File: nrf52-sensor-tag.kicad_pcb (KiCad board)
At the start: 2 copper layers, 36 x 36 mm, 20 parts, among them IC2 VEML6030, IC3 MS860702BA01-50, J3 Conn_01x07_Male, U1 MS88SF2

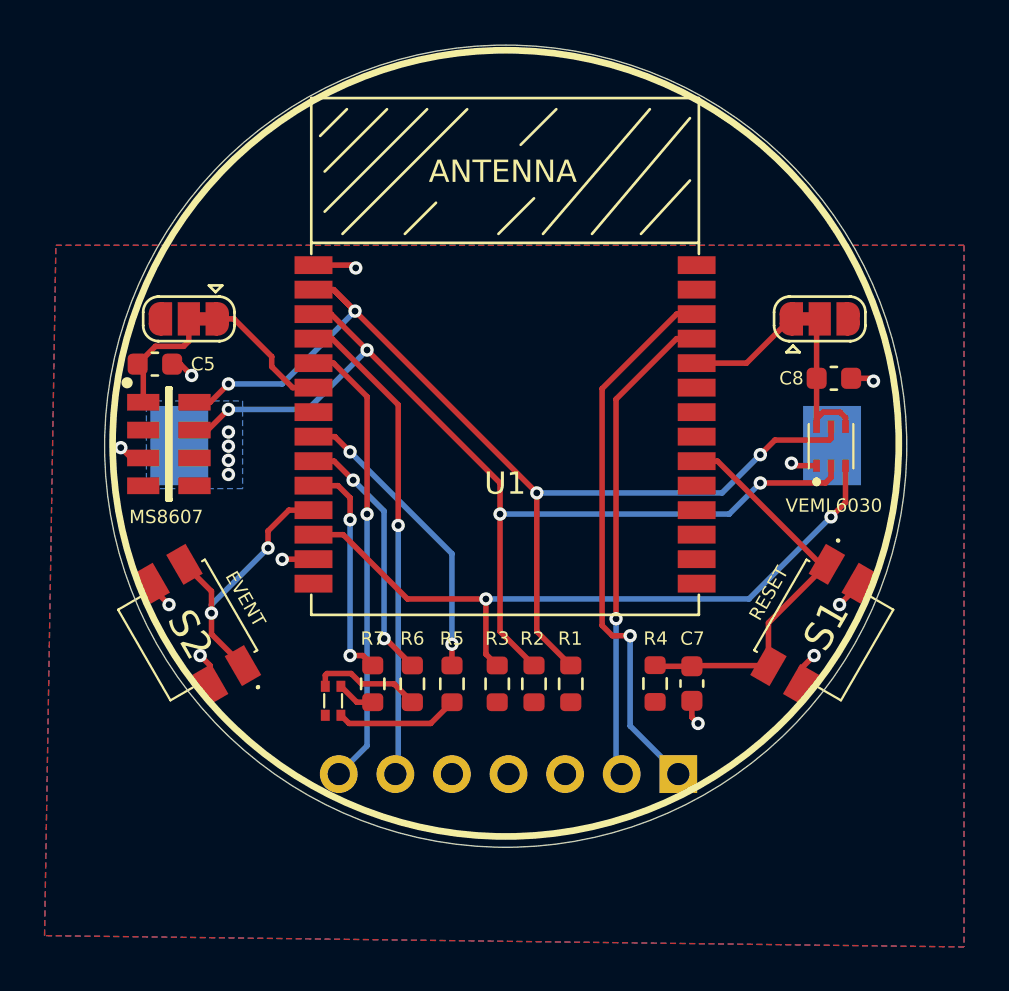
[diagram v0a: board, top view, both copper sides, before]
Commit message: #4 Sensor Tag improvements suggestions
https://github.com/HomeSmartMesh/nrf52_thread_sensortag/issues/4
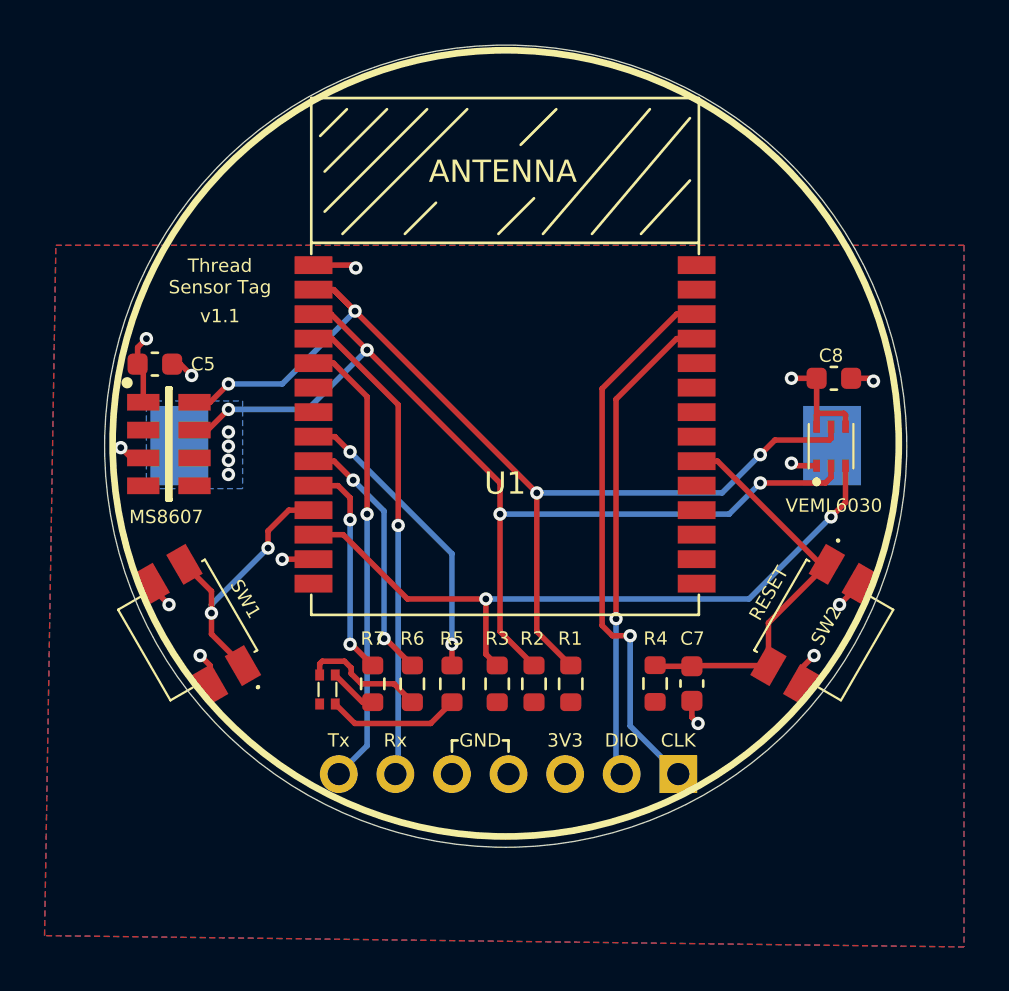
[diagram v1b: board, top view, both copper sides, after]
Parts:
- removed JP1, JP2: SolderJumper_3_Bridged12, Jumper:SolderJumper-3_P1.3mm_Bridged12_RoundedPad1.0x1.5mm
- moved LED1 0.57 mm to (113.8, 75.6)
- renumbered S2 to SW1, S1 to SW2
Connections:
- C5 pad 1: Net-(C5-Pad1) -> /VCC
- C8 pad 1: Net-(C8-Pad1) -> /VCC
- IC2 pad 4: Net-(C8-Pad1) -> /VCC
- IC2 pad 6: Net-(C8-Pad1) -> /VCC
- IC3 pad 1: Net-(C5-Pad1) -> /VCC
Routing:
- net /VCC: track 0.00 -> 8.84 mm, vias 4 -> 6
- net Net-(C8-Pad1): track 7.21 -> 0.00 mm
- net /SENS1_VCC: track 5.64 -> 0.00 mm
- net Net-(C5-Pad1): track 5.54 -> 0.00 mm
- net /SENS2_VCC: track 4.85 -> 0.00 mm
- net Net-(LED1-Pad4): track 4.97 -> 5.62 mm
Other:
- board text added: "CLK"
- board text added: "DIO"
- board text added: "SW1"
- board text removed: "DEBUG"
- board text removed: "EVENT"
- board text removed: "SWDCLK"
- board text removed: "SWDIO"
- board text removed: "UART"

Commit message: New edge cut + sensor turned by 68°
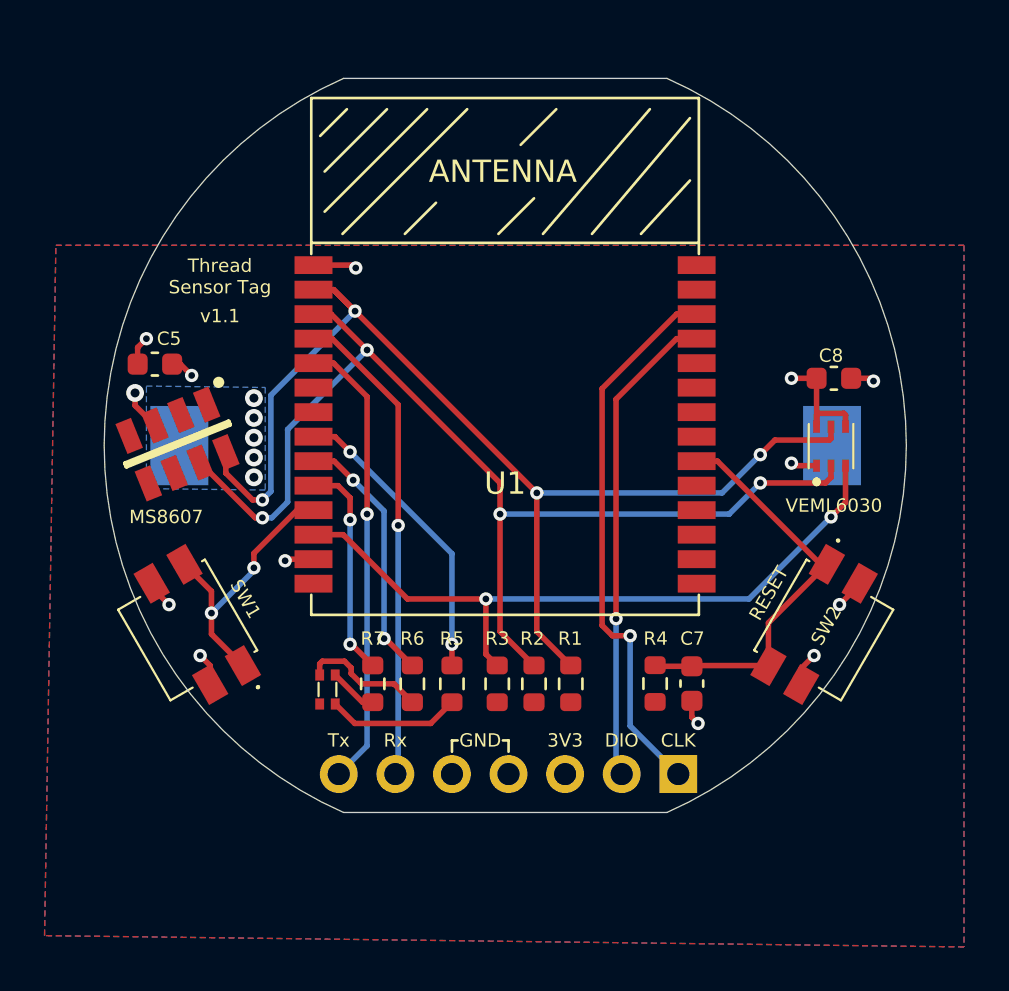
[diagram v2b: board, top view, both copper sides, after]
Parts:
- moved IC3 0.39 mm to (107.0, 64.5), turned to 292 degrees
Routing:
- net /SCL: track 47.4 -> 51.8 mm
- net /SDA: track 45.8 -> 50.2 mm
- net /VCC: track 8.84 -> 7.38 mm, vias 6 -> 7
- net GND: track 14.8 -> 15.4 mm
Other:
- board size 36 x 36 mm -> 36 x 33 mm

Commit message: Added Open Source Hardware Logo + Made in Germany + Designed with KiCad
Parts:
- added G***: LOGO, logo:mig, B.Cu at (117.9, 52.2)
- added REF**: KiCad-Logo2_5mm_SilkScreen, Symbol:KiCad-Logo2_5mm_SilkScreen, B.Cu at (122.1, 75.2)
- added REF**: OSHW-Symbol_6.7x6mm_SilkScreen, Symbol:OSHW-Symbol_6.7x6mm_SilkScreen, B.Cu at (125.9, 52.0)

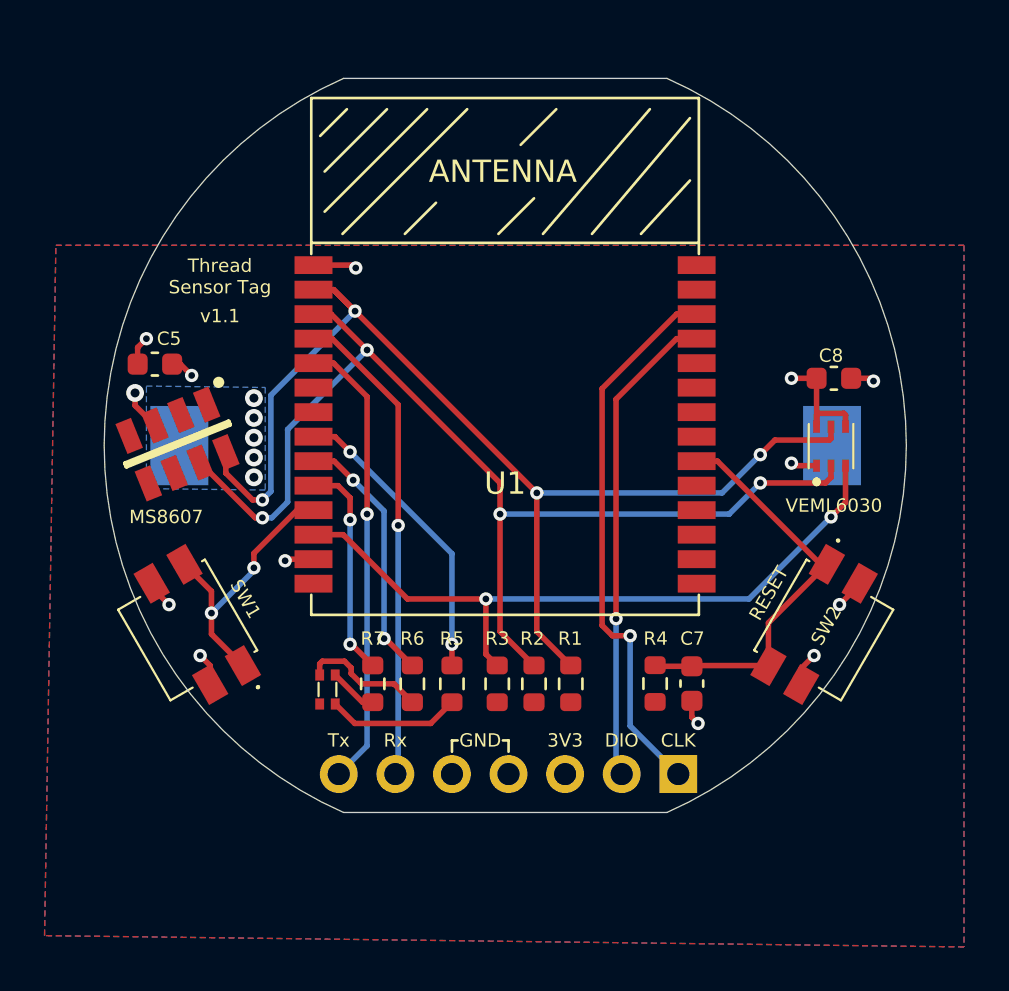
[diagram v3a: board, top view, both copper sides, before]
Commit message: Rerouting using new Battery Holder (autorouted)
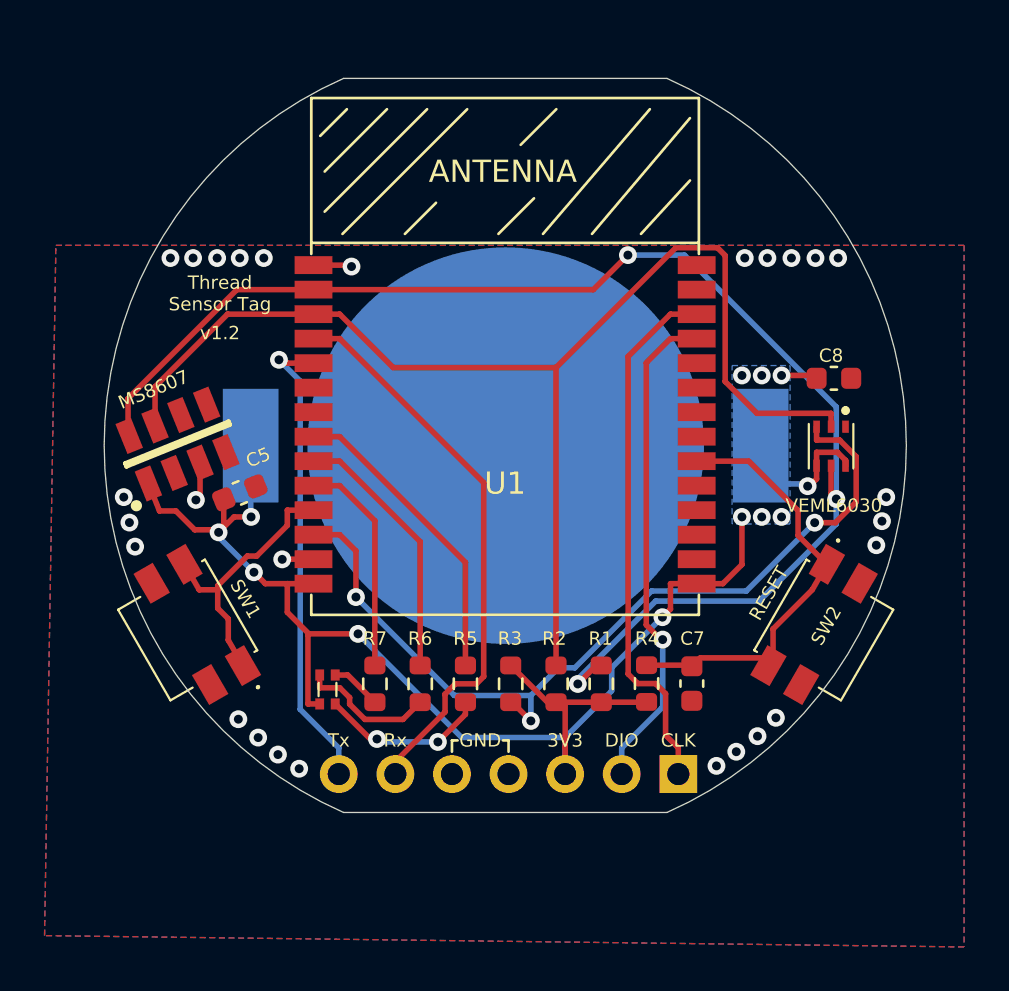
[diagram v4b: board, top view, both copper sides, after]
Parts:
- BT1: value Battery_Cell -> Battery; footprint BA2032SM:BA2032SM -> BAT-HLD-001:BATHLD001
- moved LOGO3 23.8 mm to (121.5, 51.4)
- moved LOGO2 8.75 mm to (110.2, 56.5)
- moved LOGO1 8.33 mm to (133.1, 56.1)
- moved C5 6.92 mm to (109.8, 66.7), turned to 22 degrees
- moved R1 1.37 mm to (126.1, 75.3)
- moved R2 0.99 mm to (124.0, 75.3)
- moved R3 0.61 mm to (122.0, 75.3), turned to 270 degrees
- moved R5 0.61 mm to (120.0, 75.3)
- moved R4 0.38 mm to (128.1, 75.3)
- moved R6 0.35 mm to (117.9, 75.3)
- moved R7 0.10 mm to (115.9, 75.3)
- turned IC3 to 112 degrees
- turned IC2 to 270 degrees
- renumbered REF** to LOGO1, G*** to LOGO2, REF** to LOGO3
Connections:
- net /SENS1_VCC renamed Net-(U1-Pad6)
- net /SENS2_VCC renamed Net-(U1-Pad19)
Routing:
- net /VCC: track 7.38 -> 69.4 mm, vias 7 -> 12
- net GND: track 15.4 -> 4.90 mm, vias 11 -> 27
- net /SCL: track 51.8 -> 61.9 mm, vias 4 -> 3
- net /INT1: track 31.9 -> 39.3 mm, vias 2 -> 3
- net /SDA: track 50.2 -> 57.1 mm, vias 4 -> 0
- net /Rx: track 21.9 -> 25.6 mm, vias 1 -> 0
- net Net-(LED1-Pad2): track 5.99 -> 7.61 mm, vias 0 -> 2
- net /RESET: track 18.3 -> 19.8 mm
- net /SWDCLK: track 25.0 -> 24.0 mm, vias 1 -> 0
- net /Tx: track 20.7 -> 21.3 mm
- net Net-(LED1-Pad4): track 5.62 -> 6.16 mm
- net /LED_RED: track 13.4 -> 13.8 mm, vias 2 -> 0
- net /LED_GREEN: track 11.6 -> 11.8 mm, vias 2 -> 0
- net /BTN: track 12.4 -> 12.2 mm, vias 2 -> 0
- net /LED_BLUE: track 9.85 -> 9.90 mm, vias 2 -> 0
- added copper zone on F.Cu, net GND
- removed copper zone on F.Cu, net /VCC
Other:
- board text added: "v1.2"
- board text removed: "v1.1"

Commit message: Finalized schematics + generated manufacturing files
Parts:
- BT1: value Battery -> BAT-HLD-001
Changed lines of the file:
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@@
       (effects (font (size 1.27 1.27) (thickness 0.254)) (justify mirror))
     )
-    (fp_text value Battery (at 0 0) (layer B.SilkS) hide
+    (fp_text value BAT-HLD-001 (at 0 0) (layer B.SilkS) hide
       (effects (font (size 1.27 1.27) (thickness 0.254)) (justify mirror))
     )
@@
   (module logo:mig locked (layer B.Cu)
     (at 110.2106 56.4515 180)
+    (attr virtual)
     (fp_text reference LOGO2 (at 0 0) (layer B.SilkS) hide
       (effects (font (size 1.524 1.524) (thickness 0.3)) (justify mirror))
@@
   (segment (start 113.14 56.515) (end 114.783 56.515) (width 0.25) (layer F.Cu) (net 1))
   (segment (start 114.783 56.515) (end 114.846 56.5785) (width 0.25) (layer F.Cu) (net 1))
-  (segment (start 110.318 64.6176) (end 110.318 67.7984) (width 0.25) (layer B.Cu) (net 11))
-  (segment (start 110.318 67.7984) (end 110.338 67.818) (width 0.25) (layer B.Cu) (net 11))
   (segment (start 108.046 65.3781) (end 108.046 66.8708) (width 0.25) (layer F.Cu) (net 1))
   (segment (start 108.046 66.8708) (end 107.861 67.056) (width 0.25) (layer F.Cu) (net 1))
@@
   (segment (start 111.743 69.715) (end 111.735 69.723) (width 0.25) (layer F.Cu) (net 1))
   (via (at 114.846 56.5785) (size 0.8) (layers F.Cu B.Cu) (net 1))
-  (via (at 110.338 67.818) (size 0.8) (layers F.Cu B.Cu) (net 11))
   (via (at 107.861 67.056) (size 0.8) (layers F.Cu B.Cu) (net 1))
   (via (at 111.735 69.723) (size 0.8) (layers F.Cu B.Cu) (net 1))
@@
   (segment (start 132.6766 65.315) (end 134.8938 67.5322) (width 0.25) (layer F.Cu) (net 6))
   (segment (start 130.34 65.315) (end 132.6766 65.315) (width 0.25) (layer F.Cu) (net 6))
+  (segment (start 110.318 64.6176) (end 110.318 67.7984) (width 0.25) (layer B.Cu) (net 11))
+  (segment (start 110.318 67.7984) (end 110.338 67.818) (width 0.25) (layer B.Cu) (net 11))
+  (via (at 110.338 67.818) (size 0.8) (layers F.Cu B.Cu) (net 11))
   (segment (start 124.435 77.718) (end 124.435 79.3623) (width 0.25) (layer B.Cu) (net 11))
   (segment (start 128.8032 72.3195) (end 128.7923 72.3195) (width 0.25) (layer B.Cu) (net 11))

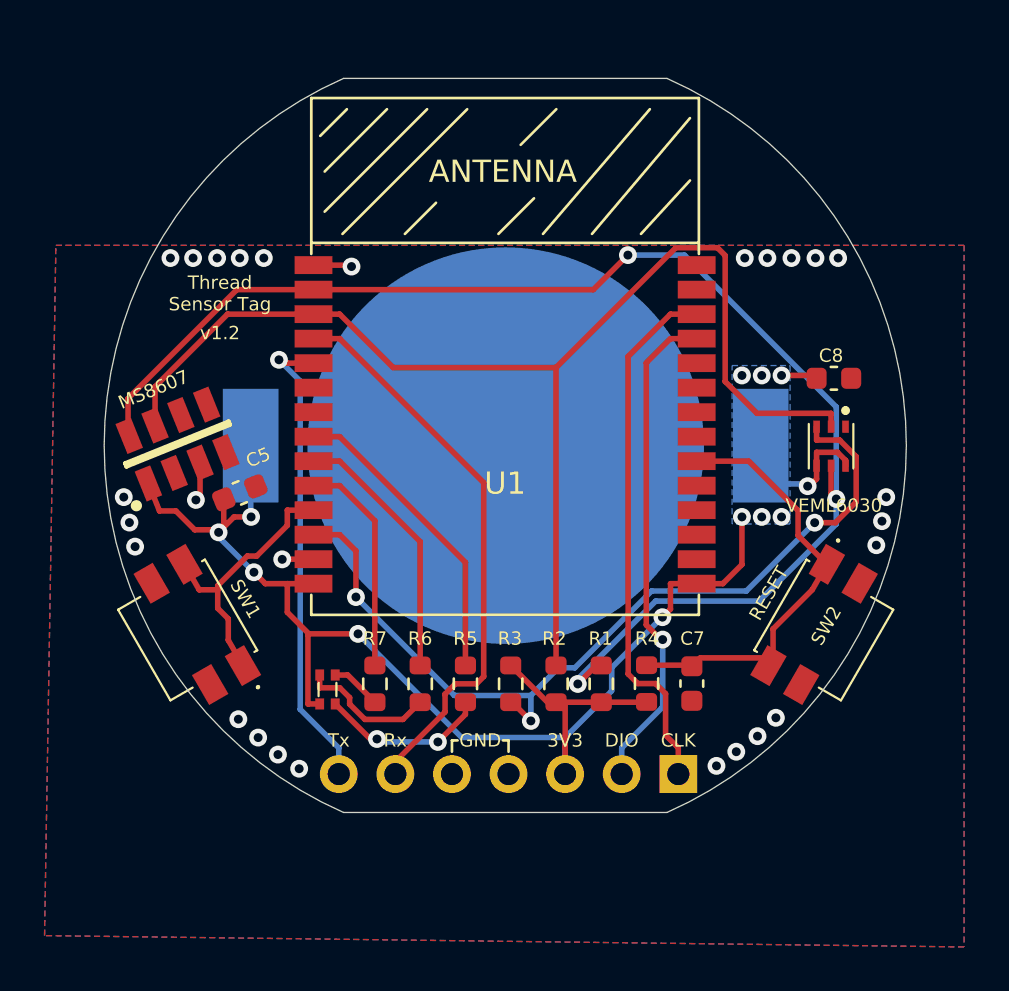
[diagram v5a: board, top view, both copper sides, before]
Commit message: Add 100uF cap + regenerated gerbers incl. F+B_Paste
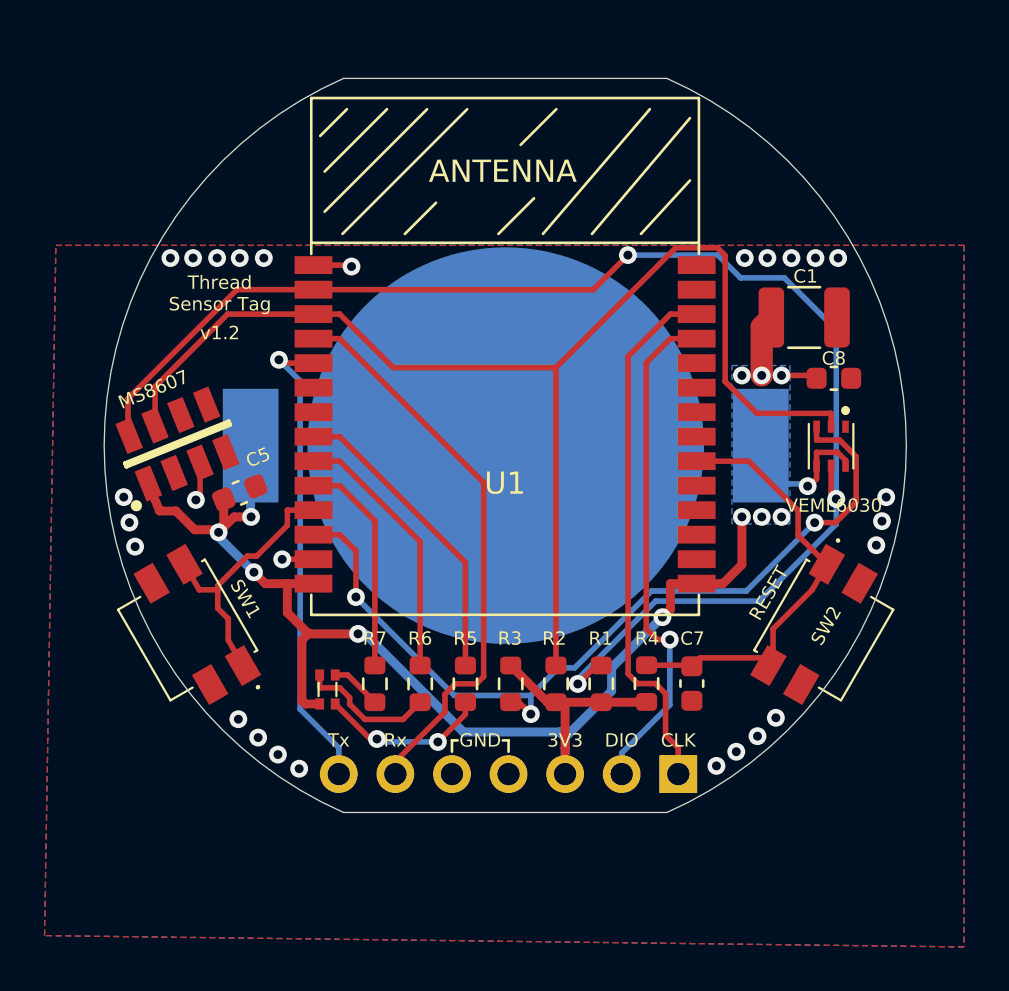
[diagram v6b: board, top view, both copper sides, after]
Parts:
- added C1: 100uF, Capacitor_SMD:C_1210_3225Metric, F.Cu at (135.2, 58.9)
- moved LOGO1 16.6 mm to (133.3, 72.8)
- moved LOGO2 16.4 mm to (111.2, 72.8)
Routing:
- net /VCC: track 69.4 -> 72.6 mm
- net /SCL: track 61.9 -> 64.0 mm
- net /SWDIO: track 22.3 -> 22.8 mm
